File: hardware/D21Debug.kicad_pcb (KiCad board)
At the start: 2 copper layers, 45.7 x 43.2 mm, 63 parts, among them J1 Micro USB, J2 Conn_01x04_Male, J3 Conn_01x04_Male, SW3 SW_Push, SW4 SW_Push, SW5 SW_Push, U1 ATSAMD21E15L-A, U2 MIC5365-3.3YC5, U3 SK9822, U4 ATSAMD21E16B-U

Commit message: Cleaned up schematic and BOM
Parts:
- D10: value (none) -> POWER
- R23, R24: value 1kΩ -> 6.8kΩ
- turned R18 to 0 degrees
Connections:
- net /A2 renamed /DBG_SWDIO
- net Net-(D11-Pad2) renamed /DBG_LED
- net Net-(D3-Pad2) renamed /LED3
- net Net-(D4-Pad2) renamed /LED4
- net Net-(D5-Pad2) renamed /LED5
- net Net-(D6-Pad2) renamed /LED6
- net Net-(J1-Pad2) renamed /USB_D-
- net Net-(J1-Pad3) renamed /USB_D+
- net Net-(J3-Pad2) renamed /DBG_SWCLK
- net Net-(R10-Pad2) renamed /SEG_B
- net Net-(R11-Pad2) renamed /SEG_C
- net Net-(R12-Pad2) renamed /SEG_D
- net Net-(R13-Pad2) renamed /SEG_E
- net Net-(R14-Pad2) renamed /SEG_F
- net Net-(R15-Pad2) renamed /SEG_G
- net Net-(R16-Pad2) renamed /SEG_DP
- net Net-(R9-Pad2) renamed /SEG_A
- net Net-(SW1-Pad1) renamed /SW1
- net Net-(SW2-Pad1) renamed /SW2
- net Net-(SW3-Pad1) renamed /SW3
- net Net-(SW4-Pad1) renamed /SW4
- C1 pad 1: Net-(C1-Pad1) -> /~{RESET}
- J2 pad 4: Net-(C1-Pad1) -> /~{RESET}
- J3 pad 4: Net-(J3-Pad4) -> /~{DBG_RESET}
- R17 pad 2: Net-(C1-Pad1) -> /~{RESET}
- R18 pad 1: Net-(C1-Pad1) -> +3V3
- R18 pad 2: +3V3 -> /~{RESET}
- R22 pad 1: Net-(J3-Pad4) -> +3V3
- R22 pad 2: +3V3 -> /~{DBG_RESET}
- U1 pad 25: Net-(C1-Pad1) -> /~{RESET}
- U4 pad E1: Net-(J3-Pad4) -> /~{DBG_RESET}
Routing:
- net Net-(C1-Pad1): track 69.9 -> 0.00 mm, vias 4 -> 0
- net /~{RESET}: track 0.00 -> 69.9 mm, vias 0 -> 4
- net Net-(J3-Pad4): track 34.1 -> 0.00 mm, vias 1 -> 0
- net /~{DBG_RESET}: track 0.00 -> 34.1 mm, vias 0 -> 1

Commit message: Forgot to save PCB
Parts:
- turned R22 to 0 degrees
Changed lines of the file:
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@@
   )
   (footprint "Resistor_SMD:R_0603_1608Metric_Pad0.98x0.95mm_HandSolder" (layer "B.Cu")
-    (at 159.004 63.119 180)
+    (at 159.004 63.119)
     (descr "Resistor SMD 0603 (1608 Metric), square (rectangular) end terminal, IPC_7351 nominal with elongated pad for handsoldering. (Body size source: IPC-SM-782 page 72, https://www.pcb-3d.com/wordpress/wp-content/uploads/ipc-sm-782a_amendment_1_and_2.pdf), generated with kicad-footprint-generator")
     (tags "resistor handsolder")
@@
     (fp_line (start -0.8 0.4125) (end 0.8 0.4125) (layer "B.Fab") (width 0.1))
     (fp_line (start -0.8 -0.4125) (end -0.8 0.4125) (layer "B.Fab") (width 0.1))
-    (pad "1" smd roundrect (at -0.9125 0 180) (size 0.975 0.95) (layers "B.Cu" "B.Paste" "B.Mask") (roundrect_rratio 0.25)
+    (pad "1" smd roundrect (at -0.9125 0) (size 0.975 0.95) (layers "B.Cu" "B.Paste" "B.Mask") (roundrect_rratio 0.25)
       (net 3 "+3V3") (pintype "passive"))
-    (pad "2" smd roundrect (at 0.9125 0 180) (size 0.975 0.95) (layers "B.Cu" "B.Paste" "B.Mask") (roundrect_rratio 0.25)
+    (pad "2" smd roundrect (at 0.9125 0) (size 0.975 0.95) (layers "B.Cu" "B.Paste" "B.Mask") (roundrect_rratio 0.25)
       (net 34 "/~{DBG_RESET}") (pintype "passive"))
     (model "${KICAD6_3DMODEL_DIR}/Resistor_SMD.3dshapes/R_0603_1608Metric.wrl"

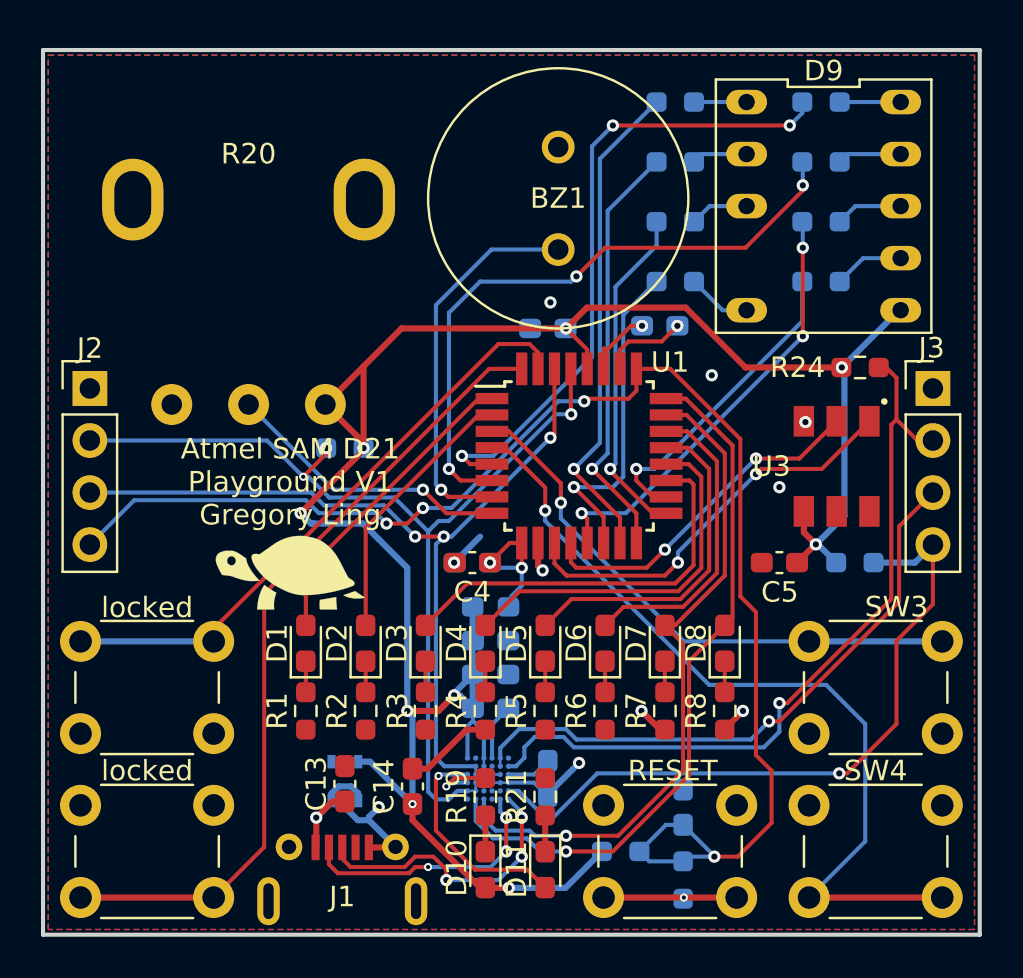
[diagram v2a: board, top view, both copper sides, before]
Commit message: Fix reset line in schematic
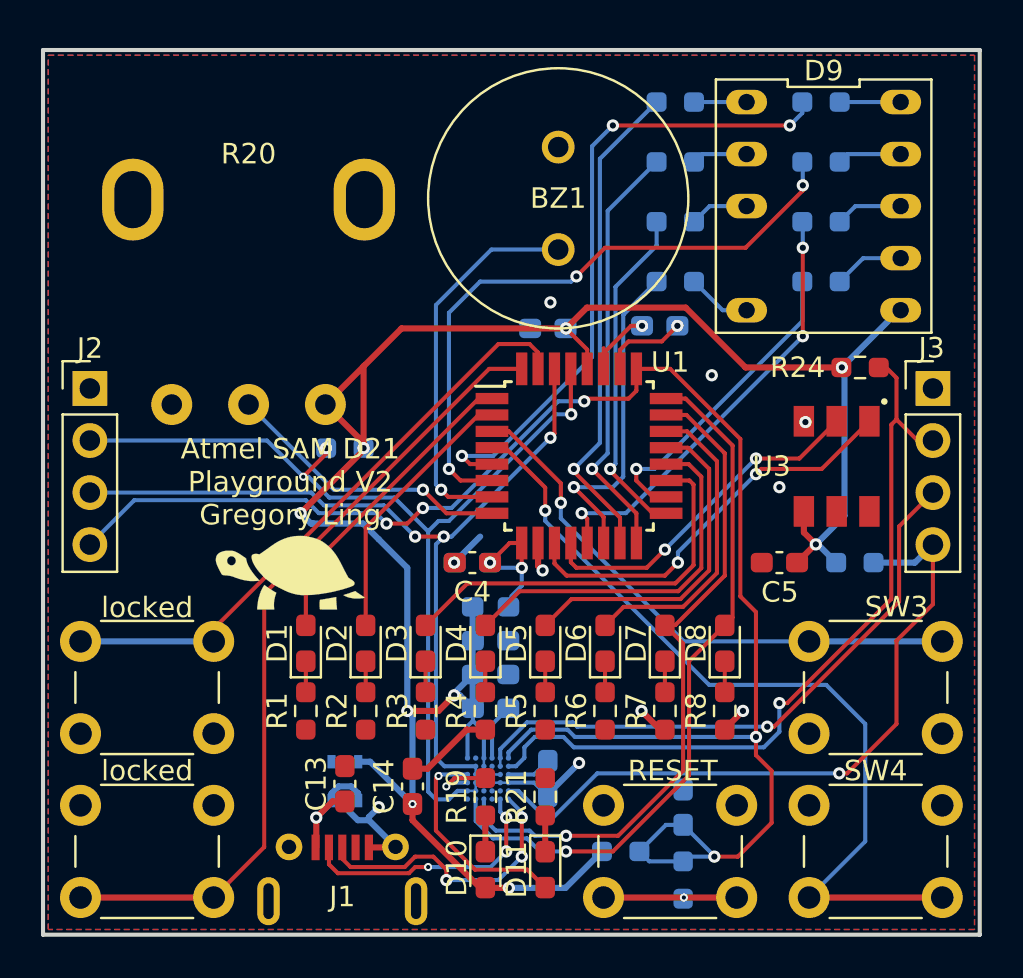
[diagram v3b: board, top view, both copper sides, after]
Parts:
- R23, R24: value 6.8kΩ -> 1kΩ
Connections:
- U4 pad A1: unconnected-(U4-PadA1) -> /~{RESET}
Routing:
- net /~{RESET}: track 69.9 -> 82.9 mm, vias 4 -> 5
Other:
- board text added: "Atmel SAM D21 Playground V2 Gregory Ling"
- board text removed: "Atmel SAM D21 Playground V1 Gregory Ling"
